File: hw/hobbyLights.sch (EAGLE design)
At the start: 60 parts, among them U1 MCP73831-2, U2 POWER, U3 BD48K28G, U4 ATMEGA32U4-AU, U5 TPS61222, Y1 RESONATORSMD

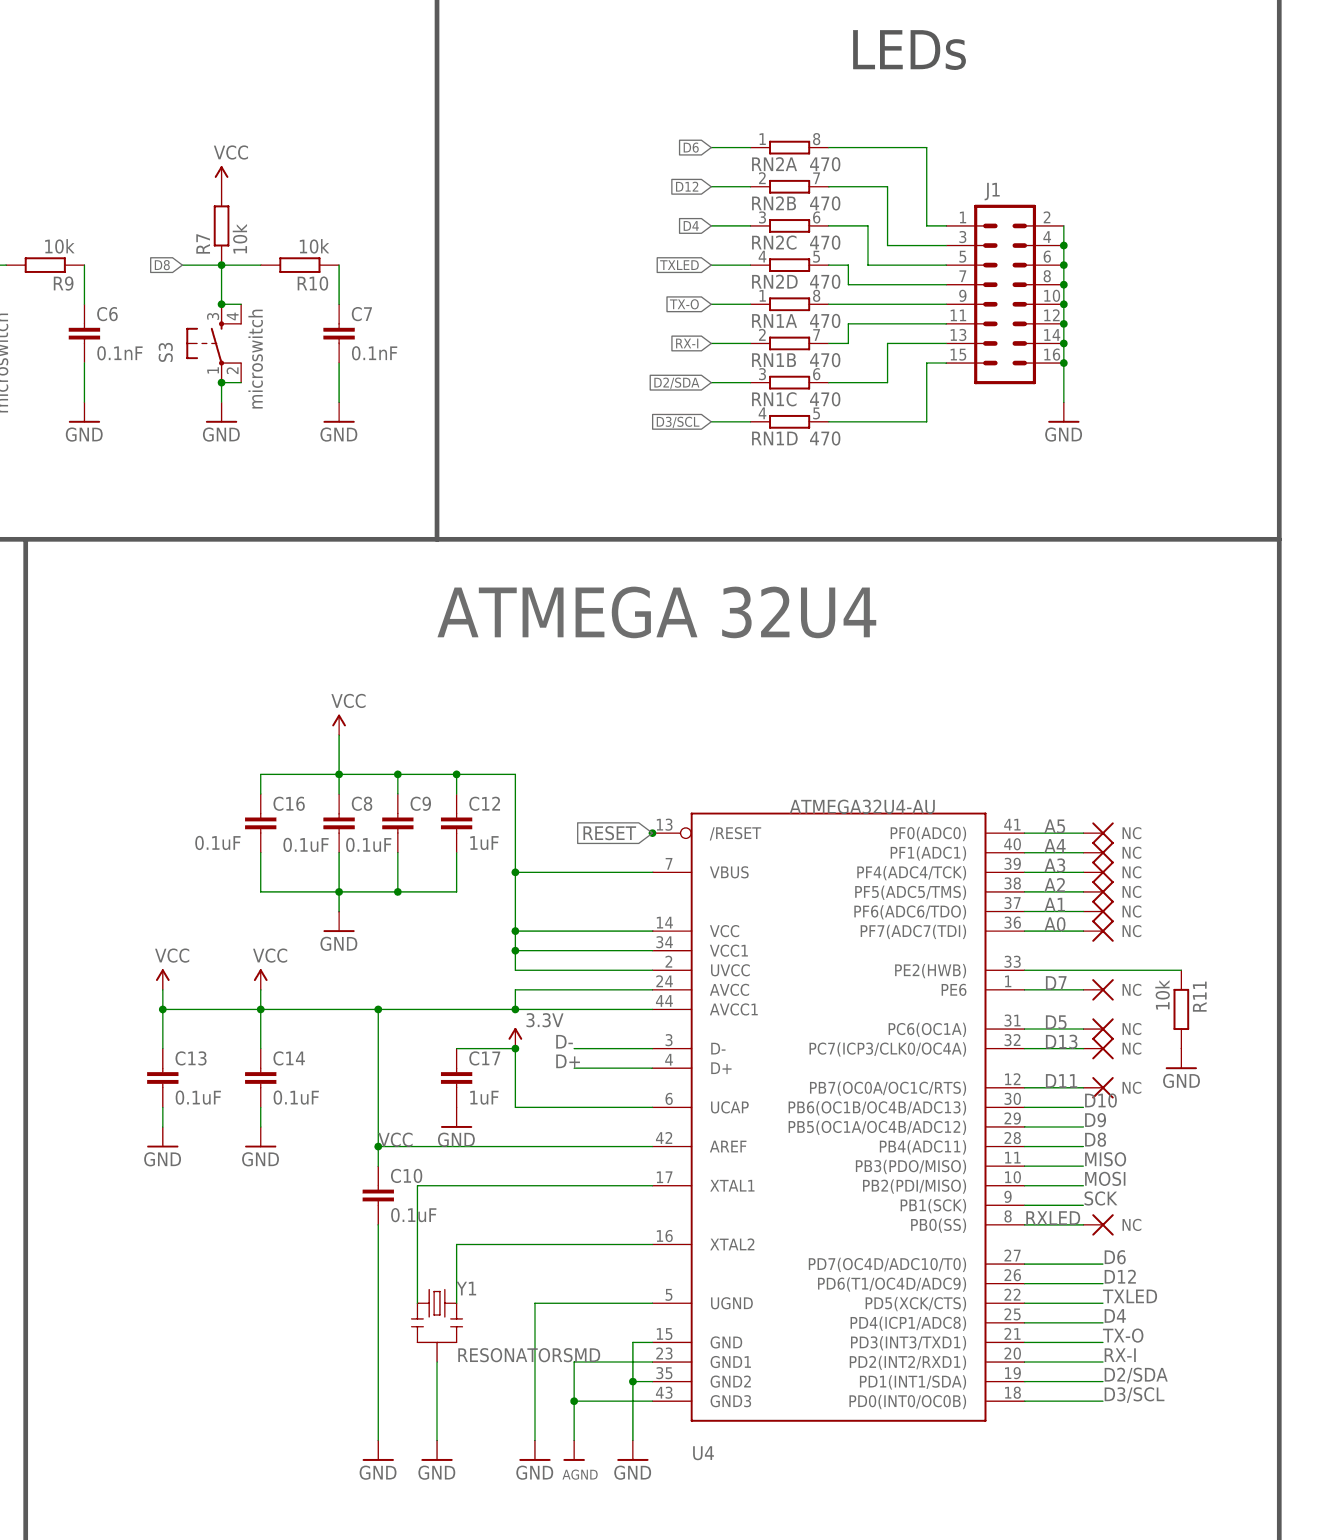
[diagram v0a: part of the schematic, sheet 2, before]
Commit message: Rev C board preparation: changed select button by trim pot, changed battery connector for JST PH RA.
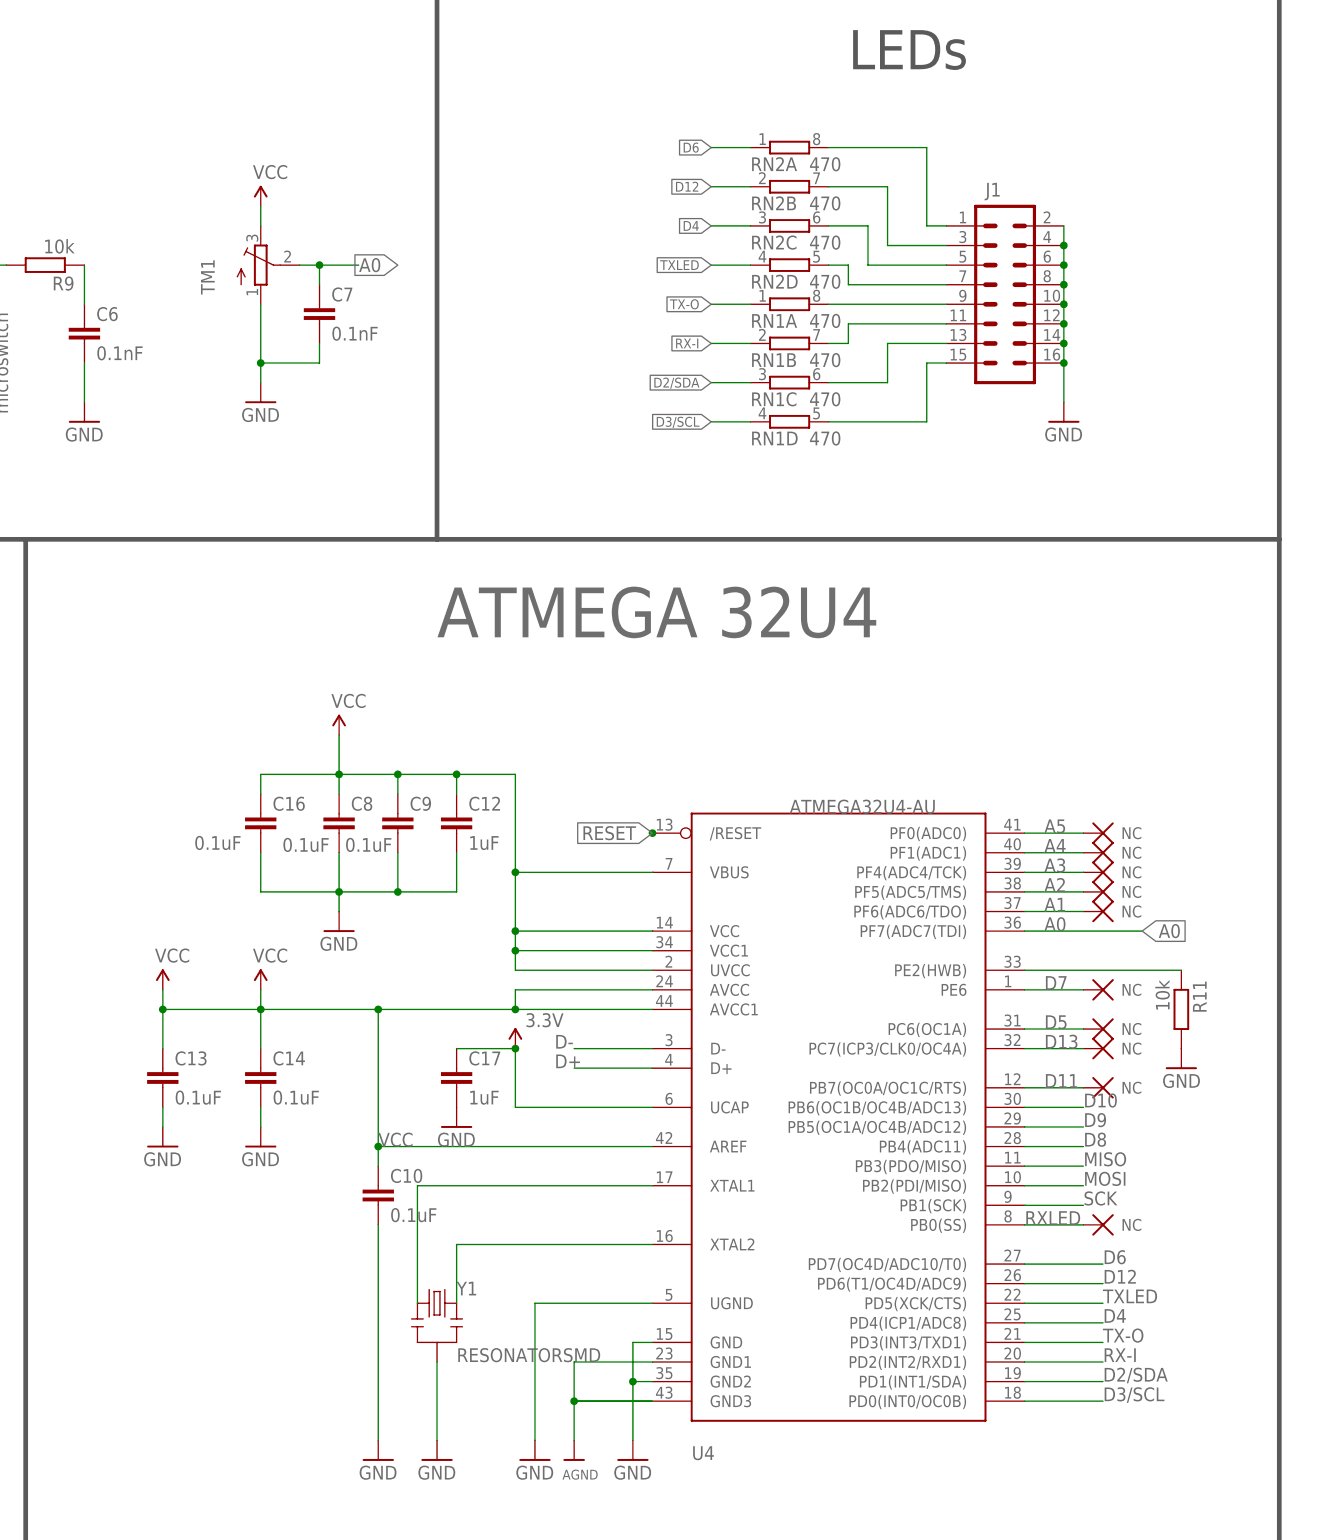
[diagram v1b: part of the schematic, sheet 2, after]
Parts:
- removed JP1: (no value), SAVLibSAV MK-I:SPARKFUN_M02POLAR
- removed R10, R7: 10k, rcl:R-EU_R0603
- removed S3: microswitch, SAVMakerI:SPARKFUN_TAC_SWITCHSMD
- removed U$17: NULL, fmc:NULL
- added CN1: (no value), adafruit:JST_2PIN-THM-RA
- added TM1: (no value), adafruit:TRIMPOTTC33X
- C10, C12, C14, C16, C17, C3, C4, C5, C6, C7, C9: device rcl:C-EUC0603 -> fmc:C-EUC0603
- R1, R11, R12, R13, R14, R2, R3, R4, R5, R6, R8, R9: device rcl:R-EU_R0603 -> fmc:R-EU_R0603
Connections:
- removed net N$10: C7.1, R10.1
- net A0: now also C7.1, TM1.S; no longer U$17.NC
- net D8: no longer R10.2, R7.1, S3.3, S3.4
- net GND: now also CN1.1, TM1.A; no longer JP1.2, S3.1, S3.2
- net VCC: now also TM1.E; no longer R7.2
- net VCCINT: now also CN1.2; no longer JP1.1
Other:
- moved on the sheet: C7

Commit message: Minor updates.
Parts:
- C13: device rcl:C-EUC0603 -> fmc:C-EUC0603
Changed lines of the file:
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@@
 <part name="S2" library="SAVMakerI" deviceset="SPARKFUN_TAC_SWITCH" device="SMD" value="microswitch"/>
 <part name="U$4" library="fmc" deviceset="AVR_ICSP" device=""/>
-<part name="C13" library="rcl" deviceset="C-EU" device="C0603" value="0.1uF"/>
+<part name="C13" library="fmc" deviceset="C-EU" device="C0603" value="0.1uF"/>
 <part name="C14" library="fmc" deviceset="C-EU" device="C0603" value="0.1uF"/>
 <part name="GND25" library="SparkFun" deviceset="GND" device=""/>

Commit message: Made adjustments to the board.
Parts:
- C8: device rcl:C-EUC0603 -> fmc:C-EUC0603
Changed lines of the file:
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@@
 <part name="MCU" library="frames" deviceset="DINA3_L" device="" value="MCU_IF"/>
 <part name="R11" library="fmc" deviceset="R-EU_" device="R0603" value="10k"/>
-<part name="C8" library="rcl" deviceset="C-EU" device="C0603" value="0.1uF"/>
+<part name="C8" library="fmc" deviceset="C-EU" device="C0603" value="0.1uF"/>
 <part name="C9" library="fmc" deviceset="C-EU" device="C0603" value="0.1uF"/>
 <part name="C10" library="fmc" deviceset="C-EU" device="C0603" value="0.1uF"/>

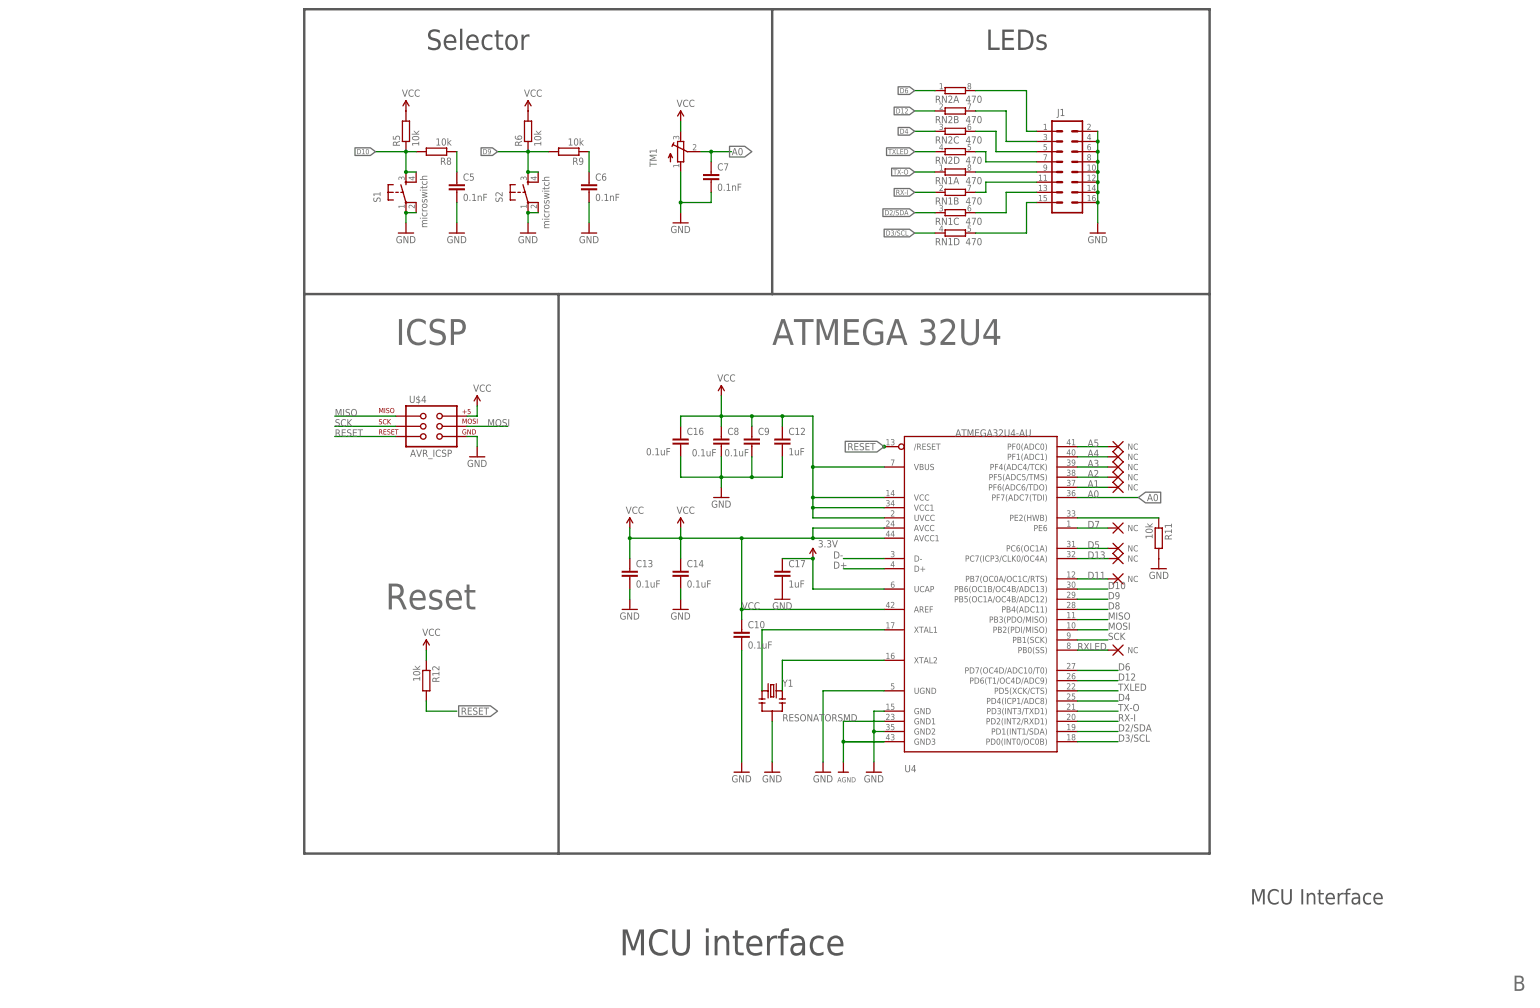
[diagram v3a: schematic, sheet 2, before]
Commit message: Added motor support.
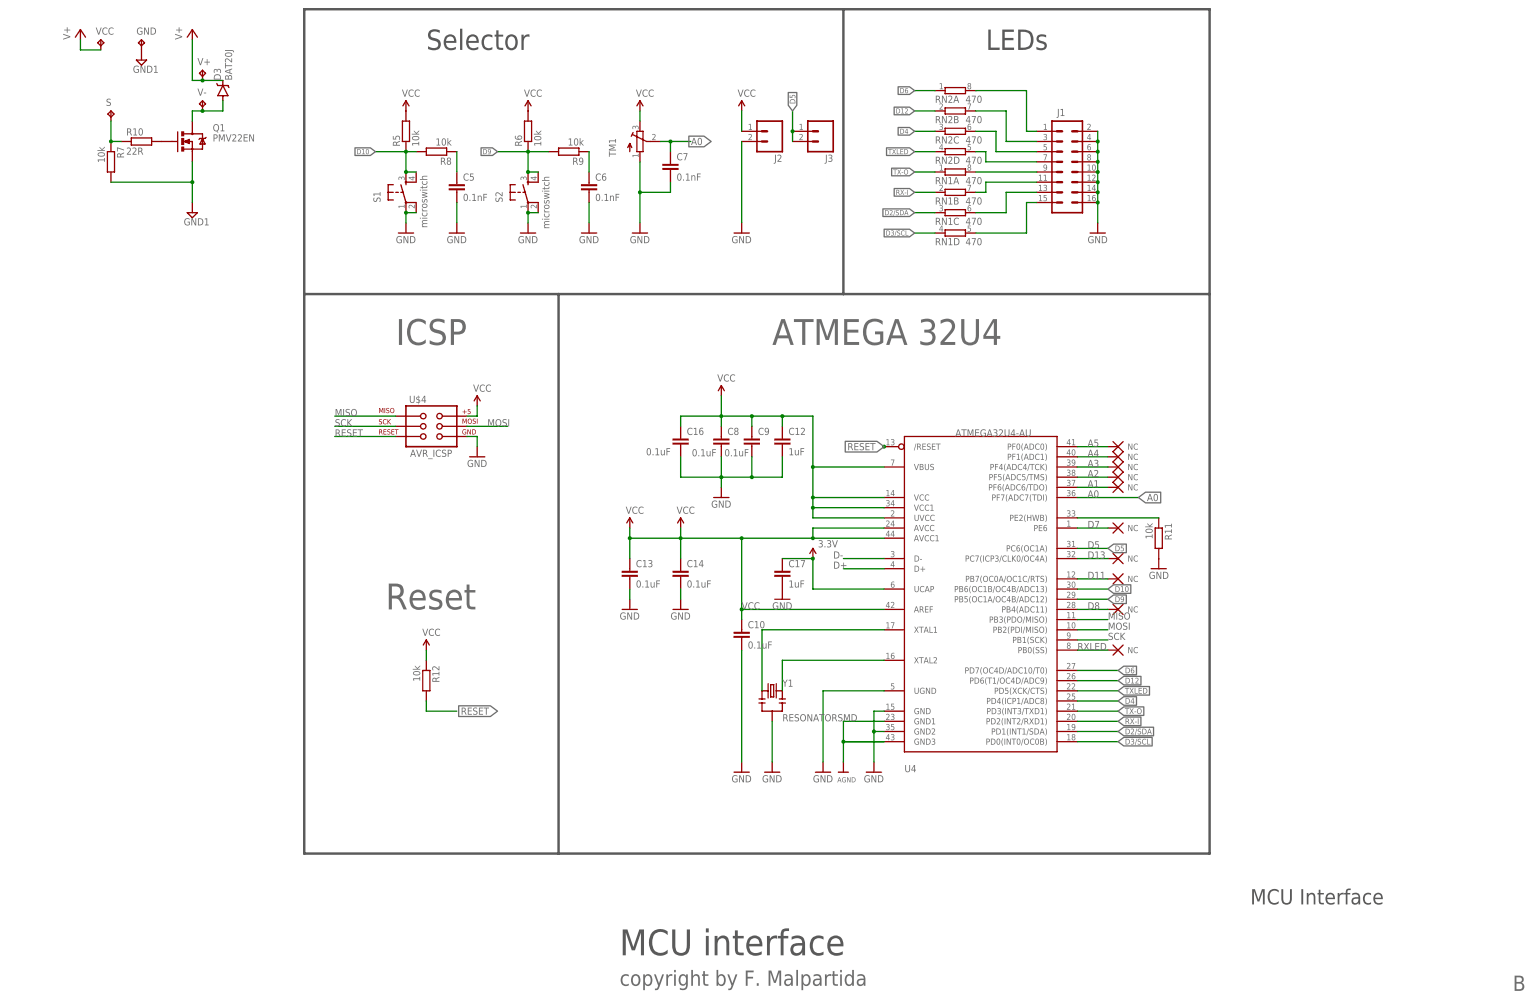
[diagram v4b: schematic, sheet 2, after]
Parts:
- removed U$20: NULL, fmc:NULL
- added D3: BAT20J, SparkFun-DiscreteSemi:DIODE-SCHOTTKY-BAT20J
- added GND, S, V+, V-, VCC: TPTP20SQ, testpad:TPTP20SQ
- added J2, J3: (no value), SparkFun-Connectors:M02PTH
- added Q1: PMV22EN, SparkFun-DiscreteSemi:MOSFET-NCHANNELAO3404A
- added R10: 22R, fmc:R-EU_R0603
- added R7: 10k, fmc:R-EU_R0603
- added U$25: NULL, fmc:NULL
- renumbered U$18 to U$6
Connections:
- new net GND1: GND.TP, Q1.S, R7.2
- new net N$1: Q1.G, R10.2
- new net N$10: D3.A, Q1.D, V-.TP
- new net N$8: R10.1, R7.1, S.TP
- new net V+: D3.C, V+.TP, VCC.TP
- net D5: now also J3.1, J3.2; no longer U$20.NC
- net D8: now also U$25.NC
- net GND: now also J2.2
- net VCC: now also J2.1
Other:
- note added: "copyright by F. Malpartida"
- moved on the sheet: C7, CN1, TM1
